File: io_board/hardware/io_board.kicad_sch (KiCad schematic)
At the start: 14 parts, among them J1 8bit_thing_bus_connector, J2 greenpak_i2c, J3 greenpak_i2c, U1 SLG46826G, U2 W65C22, U4 SLG46826G, U5 TLV73333PDBV, U6 74AHCT595

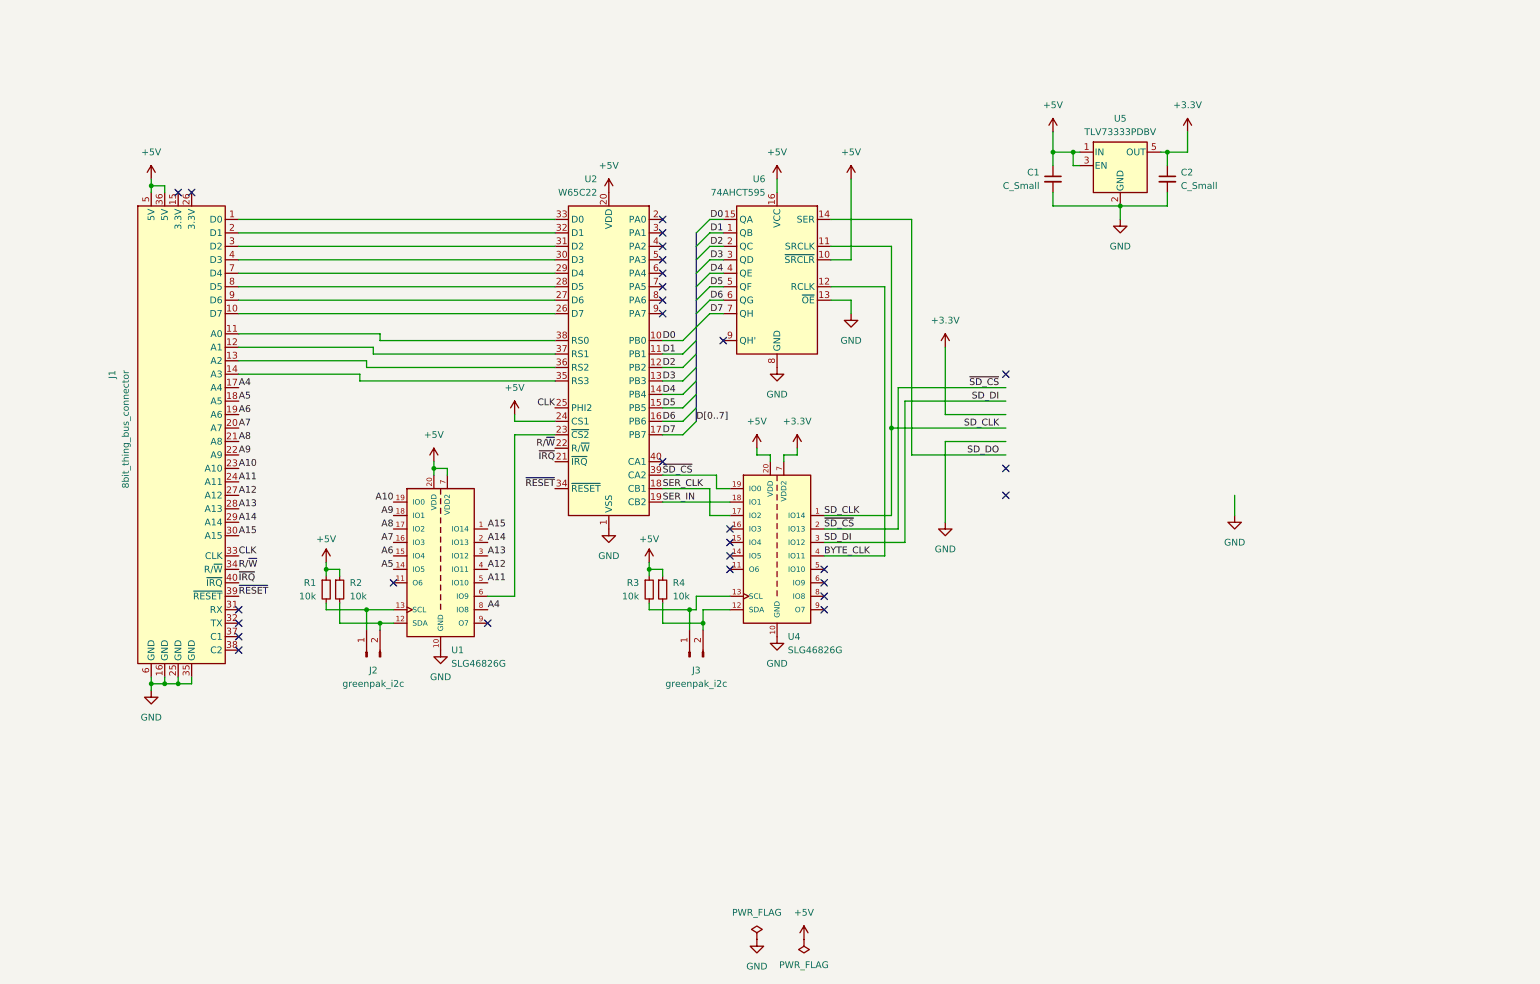
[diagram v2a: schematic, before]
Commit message: I/O Board: update schematic to add PS2 keyboard interface
This is very likely not the final pin assignment, but it's a base to start
breadboarding.
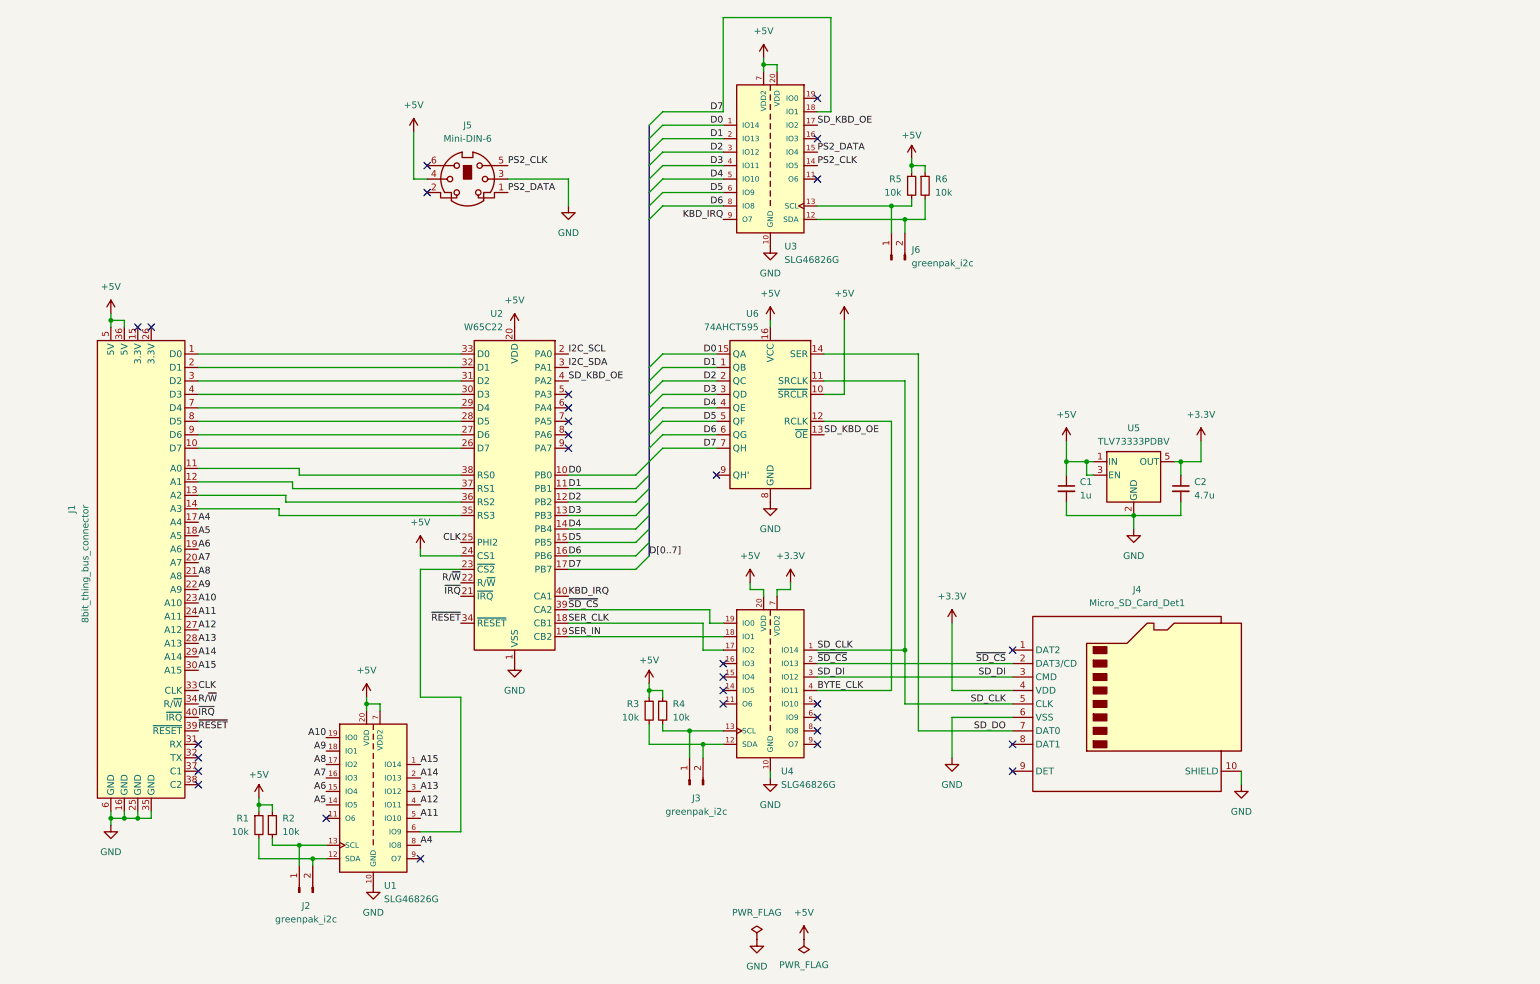
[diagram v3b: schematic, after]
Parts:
- added J4: Micro_SD_Card_Det1, symbol Connector:Micro_SD_Card_Det1
- added J5: Mini-DIN-6, symbol Connector:Mini-DIN-6
- added J6: greenpak_i2c, own_footprints:PinHeader_1x02_P2.54mm_Vertical_minimal, symbol Connector:Conn_01x02_Pin
- added R5, R6: 10k, Resistor_SMD:R_0805_2012Metric_Pad1.20x1.40mm_HandSolder, symbol Device:R_Small
- added U3: SLG46826G, SOP65P640X120-20N, symbol imported_symbols:SLG46826G
- C1: value C_Small -> 1u
- C2: value C_Small -> 4.7u
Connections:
- net +3.3V: now also J4.4 (VDD)
- net +5V: now also J5.4, R5.1, R6.1, U3.20 (VDD), U3.7 (VDD2)
- net D0: now also U3.1 (IO14)
- net D1: now also U3.2 (IO13)
- net D2: now also U3.3 (IO12)
- net D3: now also U3.4 (IO11)
- net D4: now also U3.5 (IO10)
- net D5: now also U3.6 (IO9)
- net D6: now also U3.8 (IO8)
- net D7: now also U3.18 (IO1)
- net GND: now also J4.10 (SHIELD), J4.6 (VSS), J5.3, U3.10 (GND); no longer U6.13 (~{OE})
- net SD_CLK: now also J4.5 (CLK)
- net SD_DI: now also J4.3 (CMD)
- net SD_DO: now also J4.7 (DAT0)
- net ~{SD_CS}: now also J4.2 (DAT3/CD)
- net at J2.1 (Pin_1), U1.13 (SCL): now also R2.2; no longer R1.2
- net at J2.2 (Pin_2), U1.12 (SDA): now also R1.2; no longer R2.2
- net at J3.1 (Pin_1), U4.13 (SCL): now also R4.2; no longer R3.2
- net at J3.2 (Pin_2), U4.12 (SDA): now also R3.2; no longer R4.2
- net I2C_SCL: now reaches U2.2 (PA0)
- net I2C_SDA: now reaches U2.3 (PA1)
- net SD_KBD_OE: now reaches U2.4 (PA2)
- net SD_KBD_OE: now also U6.13 (~{OE}), U3.17 (IO2)
- net KBD_IRQ: now reaches U2.40 (CA1)
- net KBD_IRQ: now also U3.9 (O7)
- new net: J6.2 (Pin_2), R6.2, U3.12 (SDA)
- new net: J6.1 (Pin_1), R5.2, U3.13 (SCL)
- new net PS2_CLK: J5.5, U3.14 (IO5)
- new net PS2_DATA: J5.1, U3.15 (IO4)
- no-connect marks 29 -> 30
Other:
- moved on the sheet: C1, C2, J1, J2, J3, R1, R2, R3, R4, U1, U2, U4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

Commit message: Update IO board schematic
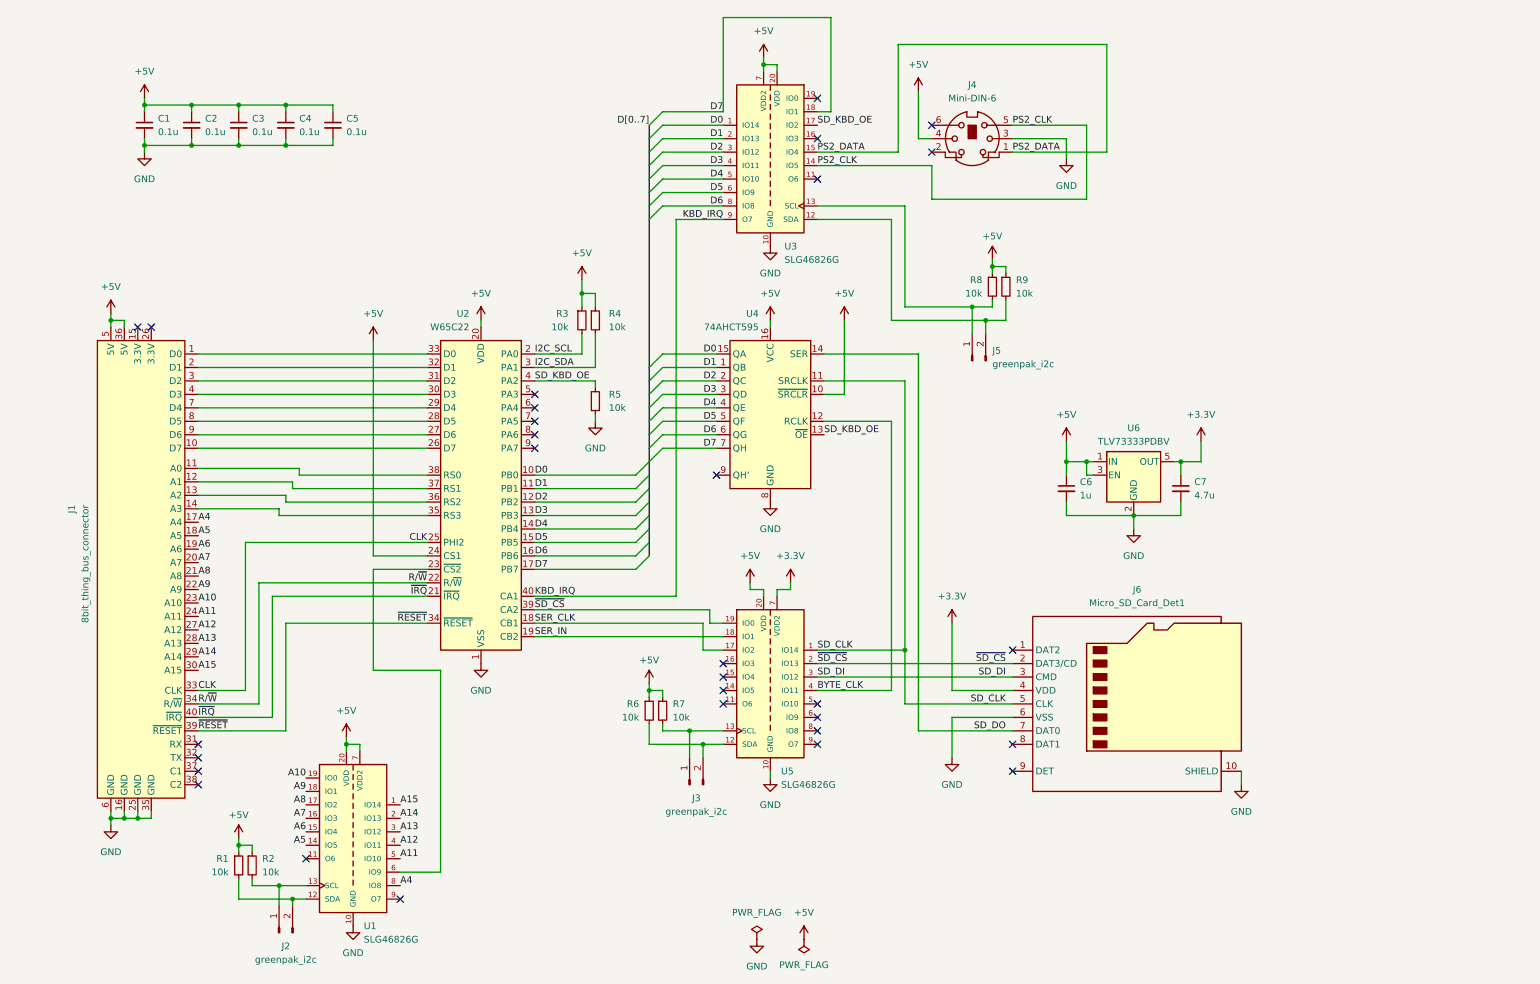
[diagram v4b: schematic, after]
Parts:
- added C1, C2, C3, C4, C5: 0.1u, symbol Device:C_Small
- added R3, R4, R5: 10k, symbol Device:R_Small
- renumbered C1 to C6, C2 to C7, J5 to J4, J6 to J5, J4 to J6, R3 to R6, R4 to R7, R5 to R8, R6 to R9, U6 to U4, U4 to U5, U5 to U6
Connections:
- net +5V: now also C1.1, C2.1, C3.1, C4.1, C5.1, R3.1, R4.1
- net GND: now also C1.2, C2.2, C3.2, C4.2, C5.2, R5.2
- net I2C_SCL: now also R3.2
- net I2C_SDA: now also R4.2
- net SD_KBD_OE: now also R5.1
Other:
- moved on the sheet: J2, J4, J5, R1, R2, R8, R9, U1, U2

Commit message: Update IO Board schematic to Kicad 9 format
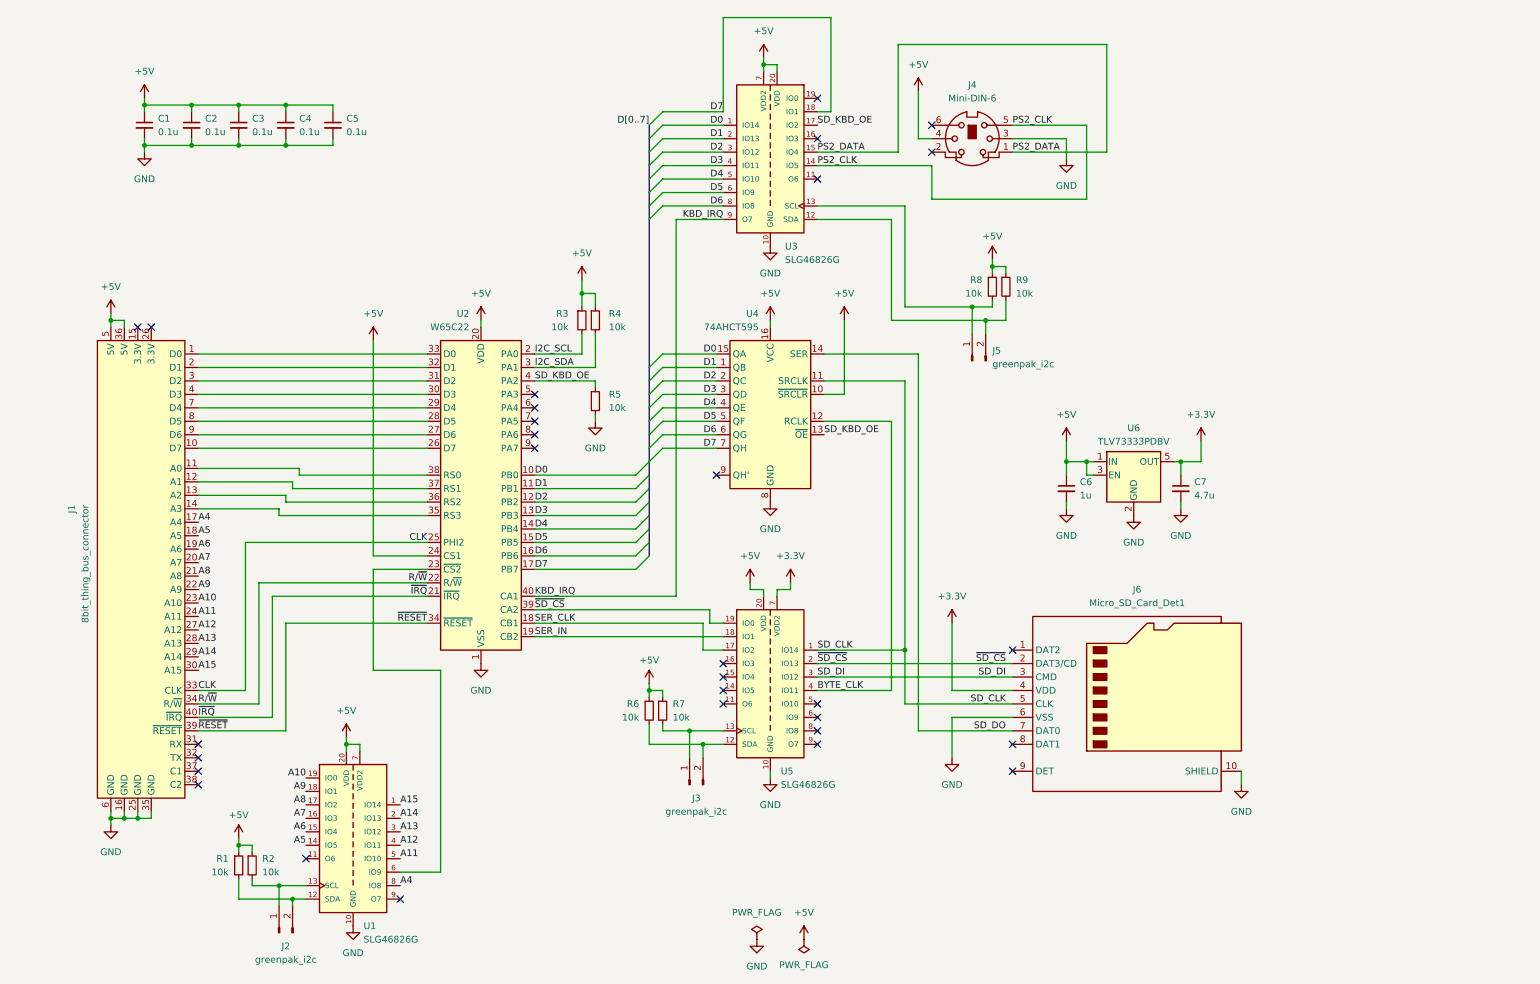
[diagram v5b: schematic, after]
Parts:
- U1, U3, U5: footprint SOP65P640X120-20N -> imported_footprints:SOP65P640X120-20N
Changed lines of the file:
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@@
 (kicad_sch
-	(version 20231120)
+	(version 20250114)
 	(generator "eeschema")
-	(generator_version "8.0")
+	(generator_version "9.0")
 	(paper "A4")
 	(junction
@@
 	)
 	(junction
-		(at 231.14 107.95)
-		(diameter 0)
-		(color 0 0 0 0)
-	)
-	(junction
 		(at 44.45 30.48)
 		(diameter 0)
@@
 	(wire
 		(pts
-			(xy 240.03 105.41) (xy 240.03 107.95)
+			(xy 240.03 105.41) (xy 240.03 106.68)
 		)
 		(stroke
@@
 	(wire
 		(pts
-			(xy 218.44 105.41) (xy 218.44 107.95)
+			(xy 218.44 105.41) (xy 218.44 106.68)
 		)
 		(stroke
@@
 	(wire
 		(pts
-			(xy 218.44 107.95) (xy 231.14 107.95)
-		)
-		(stroke
-			(width 0)
-			(type default)
-		)
-	)
-	(wire
-		(pts
 			(xy 147.32 148.59) (xy 153.67 148.59)
 		)
@@
 	(wire
 		(pts
-			(xy 231.14 110.49) (xy 231.14 107.95)
-		)
-		(stroke
-			(width 0)
-			(type default)
-		)
-	)
-	(wire
-		(pts
 			(xy 85.09 151.13) (xy 82.55 151.13)
 		)
@@
 		)
 	)
-	(wire
-		(pts
-			(xy 231.14 107.95) (xy 240.03 107.95)
-		)
-		(stroke
-			(width 0)
-			(type default)
-		)
-	)
 	(bus
 		(pts
@@
 		(fields_autoplaced yes)
 		(property "Reference" "U5"
-			(at 164.5794 156.21 0)
+			(at 164.5286 156.21 0)
 			(effects
 				(font
@@
 		)
 		(property "Value" "SLG46826G"
-			(at 164.5794 158.75 0)
+			(at 164.5286 158.75 0)
 			(effects
 				(font
@@
 			)
 		)
-		(property "Footprint" "SOP65P640X120-20N"
+		(property "Footprint" "imported_footprints:SOP65P640X120-20N"
 			(at 182.88 162.56 0)
 			(effects
@@
 		(fields_autoplaced yes)
 		(property "Reference" "U1"
-			(at 85.8394 185.42 0)
+			(at 85.7886 185.42 0)
 			(effects
 				(font
@@
 		)
 		(property "Value" "SLG46826G"
-			(at 85.8394 187.96 0)
+			(at 85.7886 187.96 0)
 			(effects
 				(font
@@
 			)
 		)
-		(property "Footprint" "SOP65P640X120-20N"
+		(property "Footprint" "imported_footprints:SOP65P640X120-20N"
 			(at 104.14 191.77 0)
 			(effects
@@
 	(symbol
 		(lib_id "power:GND")
+		(at 218.44 106.68 0)
+		(unit 1)
+		(exclude_from_sim no)
+		(in_bom yes)
+		(on_board yes)
+		(dnp no)
+		(fields_autoplaced yes)
+		(property "Reference" "#PWR034"
+			(at 218.44 113.03 0)
+			(effects
+				(font
+					(size 1.27 1.27)
+				)
+				(hide yes)
+			)
+		)
+		(property "Value" "GND"
+			(at 218.44 111.76 0)
+			(effects
+				(font
+					(size 1.27 1.27)
+				)
+			)
+		)
+		(property "Footprint" ""
+			(at 218.44 106.68 0)
+			(effects
+				(font
+					(size 1.27 1.27)
+				)
+				(hide yes)
+			)
+		)
+		(property "Datasheet" ""
+			(at 218.44 106.68 0)
+			(effects
+				(font
+					(size 1.27 1.27)
+				)
+				(hide yes)
+			)
+		)
+		(property "Description" "Power symbol creates a global label with name \"GND\" , ground"
+			(at 218.44 106.68 0)
+			(effects
+				(font
+					(size 1.27 1.27)
+				)
+				(hide yes)
+			)
+		)
+		(pin "1"
+		)
+		(instances
+			(project "io_board"
+				(path "/9a0d46a3-4768-4dac-8f10-2d7145cbddfa"
+					(reference "#PWR034")
+					(unit 1)
+				)
+			)
+		)
+	)
+	(symbol
+		(lib_id "power:GND")
+		(at 240.03 106.68 0)
+		(unit 1)
+		(exclude_from_sim no)
+		(in_bom yes)
+		(on_board yes)
+		(dnp no)
+		(fields_autoplaced yes)
+		(property "Reference" "#PWR033"
+			(at 240.03 113.03 0)
+			(effects
+				(font
+					(size 1.27 1.27)
+				)
+				(hide yes)
+			)
+		)
+		(property "Value" "GND"
+			(at 240.03 111.76 0)
+			(effects
+				(font
+					(size 1.27 1.27)
+				)
+			)
+		)
+		(property "Footprint" ""
+			(at 240.03 106.68 0)
+			(effects
+				(font
+					(size 1.27 1.27)
+				)
+				(hide yes)
+			)
+		)
+		(property "Datasheet" ""
+			(at 240.03 106.68 0)
+			(effects
+				(font
+					(size 1.27 1.27)
+				)
+				(hide yes)
+			)
+		)
+		(property "Description" "Power symbol creates a global label with name \"GND\" , ground"
+			(at 240.03 106.68 0)
+			(effects
+				(font
+					(size 1.27 1.27)
+				)
+				(hide yes)
+			)
+		)
+		(pin "1"
+		)
+		(instances
+			(project "io_board"
+				(path "/9a0d46a3-4768-4dac-8f10-2d7145cbddfa"
+					(reference "#PWR033")
+					(unit 1)
+				)
+			)
+		)
+	)
+	(symbol
+		(lib_id "power:GND")
 		(at 129.54 90.17 0)
 		(unit 1)
@@
 	(symbol
 		(lib_id "power:GND")
-		(at 231.14 110.49 0)
+		(at 231.14 107.95 0)
 		(unit 1)
 		(exclude_from_sim no)
@@
 		(fields_autoplaced yes)
 		(property "Reference" "#PWR030"
-			(at 231.14 116.84 0)
+			(at 231.14 114.3 0)
 			(effects
 				(font
@@
 		)
 		(property "Value" "GND"
-			(at 231.14 115.57 0)
+			(at 231.14 113.03 0)
 			(effects
 				(font
@@
 		)
 		(property "Footprint" ""
-			(at 231.14 110.49 0)
+			(at 231.14 107.95 0)
 			(effects
 				(font
@@
 		)
 		(property "Datasheet" ""
-			(at 231.14 110.49 0)
+			(at 231.14 107.95 0)
 			(effects
 				(font
@@
 		)
 		(property "Description" "Power symbol creates a global label with name \"GND\" , ground"
-			(at 231.14 110.49 0)
+			(at 231.14 107.95 0)
 			(effects
 				(font
@@
 		(fields_autoplaced yes)
 		(property "Reference" "U3"
-			(at 165.2271 57.15 0)
+			(at 165.3287 57.15 0)
 			(effects
 				(font
@@
 		)
 		(property "Value" "SLG46826G"
-			(at 165.2271 59.69 0)
+			(at 165.3287 59.69 0)
 			(effects
 				(font
@@
 			)
 		)
-		(property "Footprint" "SOP65P640X120-20N"
+		(property "Footprint" "imported_footprints:SOP65P640X120-20N"
 			(at 142.24 63.5 0)
 			(effects
@@
 		)
 	)
+	(embedded_fonts no)
 )
